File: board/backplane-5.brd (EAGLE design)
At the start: 100 x 100 mm, 142 parts, among them CN1 RJ45JACK90, U1 AMS1117-5.0, U10 RT9193, U11 KSZ9897, U12 KSZ8081MLX, U2 AMS1117-5.0, U3 AMS1117-5.0, U4 AMS1117-5.0, U5 AMS1117-5.0, U6 AMS1117-2.5, U7 AMS1117-1.2, U8 RT9193, U9 AMS1117-5.0, X1 25MHz, X2 25MHz

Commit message: Routed the MII interface
Holy shit.
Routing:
- net PHY6-CRS: track 0.00 -> 23.3 mm, vias 0 -> 2
- net PHY6-RXD0: track 0.00 -> 22.8 mm, vias 0 -> 2
- net PHY6-RXD2: track 0.00 -> 22.5 mm, vias 0 -> 2
- net PHY6-RXD1: track 0.00 -> 22.3 mm, vias 0 -> 2
- net PHY6-RXD3: track 0.00 -> 22.3 mm, vias 0 -> 2
- net PHY6-COL: track 0.00 -> 21.9 mm
- net PHY6-TXD3: track 0.00 -> 21.2 mm
- net PHY6-TXD2: track 0.00 -> 20.6 mm
- net PHY6-TXC: track 0.00 -> 16.9 mm, vias 0 -> 2
- net PHY6-RXER: track 0.00 -> 16.6 mm, vias 0 -> 2
- net PHY6-TXD1: track 0.00 -> 16.4 mm
- net PHY6-TXD0: track 0.00 -> 16.4 mm
- net PHY6-TXEN: track 0.00 -> 15.9 mm, vias 0 -> 2
- net PHY6-RXC: track 0.00 -> 15.7 mm
- net PHY6-RXDV: track 0.00 -> 15.6 mm
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
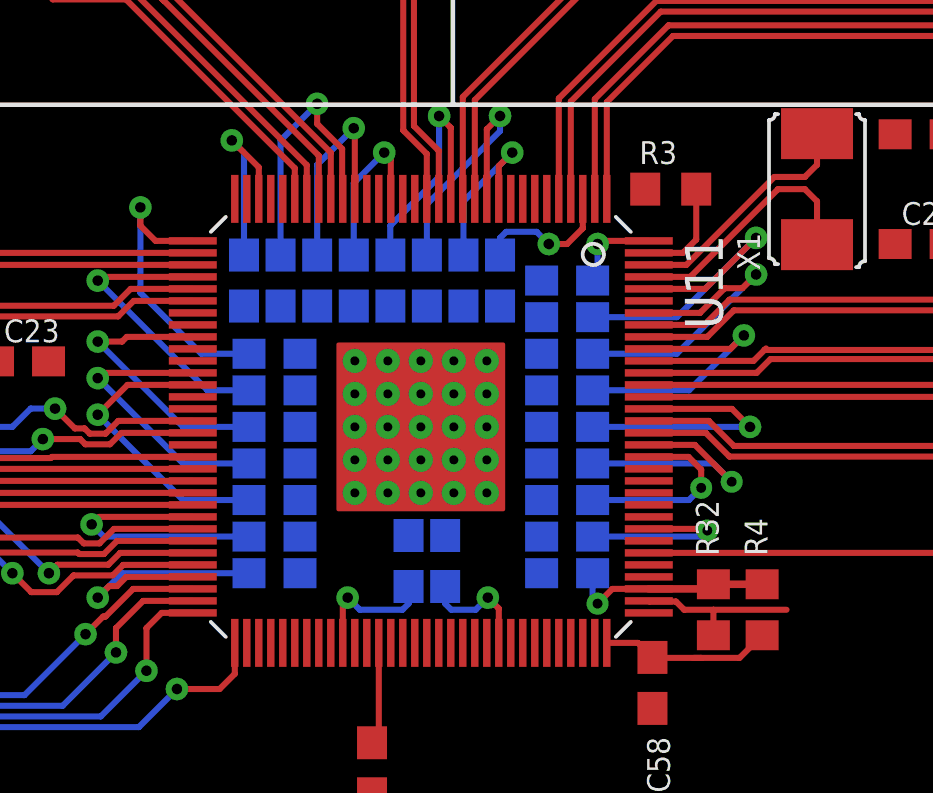
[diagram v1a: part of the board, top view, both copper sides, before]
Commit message: Tweaked some decoupling caps
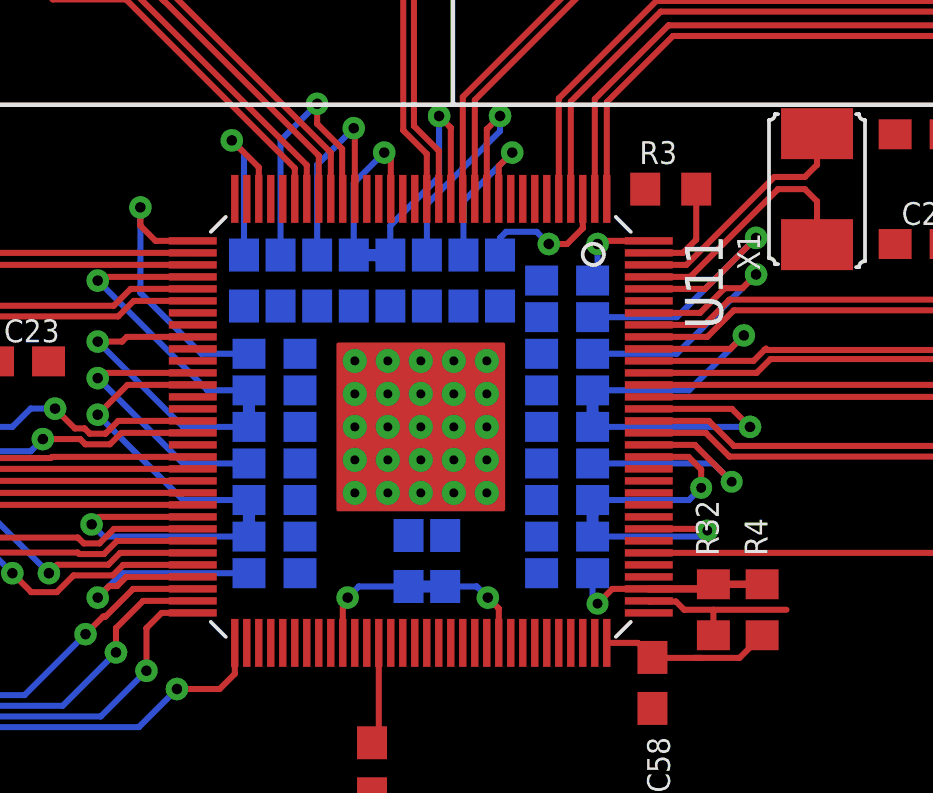
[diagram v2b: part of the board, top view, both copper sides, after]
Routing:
- net 1V2-A: track 72.9 -> 76.5 mm
- net 1V2: track 64.2 -> 66.5 mm
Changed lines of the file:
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@@
 <via x="68.4784" y="25.8064" extent="1-16" drill="0.3302"/>
 <via x="68.2752" y="27.2288" extent="1-16" drill="0.3302"/>
-<wire x1="64.6548" y1="25.6032" x2="68.2752" y2="25.6032" width="0.2032" layer="16"/>
+<wire x1="68.2752" y1="25.6032" x2="64.6548" y2="25.6032" width="0.2032" layer="16"/>
 <wire x1="68.2752" y1="25.6032" x2="68.4784" y2="25.8064" width="0.2032" layer="16"/>
 <wire x1="66.528" y1="25.8608" x2="68.424" y2="25.8608" width="0.2032" layer="1"/>
@@
 <wire x1="51.328" y1="30.6608" x2="49.152" y2="30.6608" width="0.2032" layer="1"/>
 <wire x1="49.152" y1="30.6608" x2="48.1584" y2="29.6672" width="0.2032" layer="1"/>
-<wire x1="53.2012" y1="26.8224" x2="51.0032" y2="26.8224" width="0.2032" layer="16"/>
+<wire x1="51.0032" y1="26.8224" x2="53.2012" y2="26.8224" width="0.2032" layer="16"/>
 <wire x1="51.0032" y1="26.8224" x2="48.1584" y2="29.6672" width="0.2032" layer="16"/>
 <via x="55.4736" y="40.0304" extent="1-16" drill="0.35"/>
@@
 <via x="61.1632" y="23.5712" extent="1-16" drill="0.35"/>
 <via x="56.4896" y="23.5712" extent="1-16" drill="0.35"/>
-<wire x1="58.5216" y1="23.9404" x2="58.5216" y2="23.368" width="0.2032" layer="16"/>
-<wire x1="58.5216" y1="23.368" x2="58.3184" y2="23.1648" width="0.2032" layer="16"/>
-<wire x1="58.3184" y1="23.1648" x2="56.896" y2="23.1648" width="0.2032" layer="16"/>
-<wire x1="56.896" y1="23.1648" x2="56.4896" y2="23.5712" width="0.2032" layer="16"/>
 <wire x1="56.328" y1="22.0608" x2="56.328" y2="23.4096" width="0.2032" layer="1"/>
 <wire x1="56.328" y1="23.4096" x2="56.4896" y2="23.5712" width="0.2032" layer="1"/>
-<wire x1="59.7408" y1="23.9404" x2="59.7408" y2="23.368" width="0.2032" layer="16"/>
-<wire x1="59.7408" y1="23.368" x2="59.944" y2="23.1648" width="0.2032" layer="16"/>
-<wire x1="59.944" y1="23.1648" x2="60.7568" y2="23.1648" width="0.2032" layer="16"/>
-<wire x1="60.7568" y1="23.1648" x2="61.1632" y2="23.5712" width="0.2032" layer="16"/>
 <wire x1="61.528" y1="22.0608" x2="61.528" y2="23.2064" width="0.2032" layer="1"/>
 <wire x1="61.528" y1="23.2064" x2="61.1632" y2="23.5712" width="0.2032" layer="1"/>
@@
 <wire x1="48.3616" y1="25.6032" x2="47.9552" y2="26.0096" width="0.2032" layer="16"/>
 <wire x1="53.2012" y1="25.6032" x2="48.3616" y2="25.6032" width="0.2032" layer="16"/>
+<wire x1="64.6548" y1="25.6032" x2="64.6548" y2="26.8224" width="0.4064" layer="16"/>
+<wire x1="53.2012" y1="26.8224" x2="53.2012" y2="25.6032" width="0.4064" layer="16"/>
+<wire x1="58.5216" y1="23.9404" x2="59.7408" y2="23.9404" width="0.4064" layer="16"/>
+<wire x1="58.5216" y1="23.9404" x2="56.8588" y2="23.9404" width="0.2032" layer="16"/>
+<wire x1="56.8588" y1="23.9404" x2="56.4896" y2="23.5712" width="0.2032" layer="16"/>
+<wire x1="59.7408" y1="23.9404" x2="60.794" y2="23.9404" width="0.2032" layer="16"/>
+<wire x1="60.794" y1="23.9404" x2="61.1632" y2="23.5712" width="0.2032" layer="16"/>
 <wire x1="-98.64" y1="-285.75" x2="-76.07" y2="-118.11" width="0" layer="19" extent="1-1"/>
 <wire x1="23.6084" y1="28.8544" x2="-76.07" y2="-118.11" width="0" layer="19" extent="1-1"/>
 <wire x1="35.9492" y1="27.0724" x2="27.4492" y2="28.0724" width="0" layer="19" extent="1-1"/>
 <wire x1="47.9552" y1="26.0096" x2="38.9772" y2="27.2288" width="0" layer="19" extent="1-1"/>
-<wire x1="51.0032" y1="26.8224" x2="51.328" y2="26.2608" width="0" layer="19" extent="1-16"/>
 <wire x1="56.328" y1="23.4096" x2="53.2012" y2="25.6032" width="0" layer="19" extent="1-16"/>
-<wire x1="59.7408" y1="23.9404" x2="58.5216" y2="23.9404" width="0" layer="19" extent="16-16"/>
 <wire x1="64.6548" y1="25.6032" x2="61.528" y2="23.2064" width="0" layer="19" extent="1-16"/>
-<wire x1="67.8688" y1="26.8224" x2="68.424" y2="25.8608" width="0" layer="19" extent="1-16"/>
 <wire x1="54.2544" y1="34.9876" x2="51.328" y2="30.6608" width="0" layer="19" extent="1-16"/>
 <wire x1="59.1312" y1="36.6827" x2="56.328" y2="36.8608" width="0" layer="19" extent="1-16"/>
@@
 <wire x1="66.528" y1="29.8608" x2="69.3008" y2="29.8608" width="0.2032" layer="1"/>
 <wire x1="69.3008" y1="29.8608" x2="69.9008" y2="29.2608" width="0.2032" layer="1"/>
-<wire x1="64.6548" y1="29.2608" x2="69.9008" y2="29.2608" width="0.2032" layer="16"/>
+<wire x1="69.9008" y1="29.2608" x2="64.6548" y2="29.2608" width="0.2032" layer="16"/>
 <via x="69.6976" y="32.3088" extent="1-16" drill="0.35"/>
 <wire x1="66.528" y1="31.8608" x2="69.2496" y2="31.8608" width="0.2032" layer="1"/>
@@
 <wire x1="51.328" y1="34.2608" x2="48.2816" y2="34.2608" width="0.2032" layer="1"/>
 <wire x1="48.2816" y1="34.2608" x2="48.1584" y2="34.1376" width="0.2032" layer="1"/>
-<wire x1="53.2012" y1="30.48" x2="51.816" y2="30.48" width="0.2032" layer="16"/>
+<wire x1="51.816" y1="30.48" x2="53.2012" y2="30.48" width="0.2032" layer="16"/>
 <wire x1="51.816" y1="30.48" x2="48.1584" y2="34.1376" width="0.2032" layer="16"/>
 <via x="52.6288" y="38.8112" extent="1-16" drill="0.35"/>
@@
 <wire x1="57.928" y1="36.8608" x2="57.928" y2="38.1856" width="0.2032" layer="1"/>
 <wire x1="57.928" y1="38.1856" x2="57.7088" y2="38.4048" width="0.2032" layer="1"/>
-<wire x1="56.6928" y1="34.9876" x2="56.6928" y2="37.3888" width="0.2032" layer="16"/>
+<wire x1="56.6928" y1="37.3888" x2="56.6928" y2="34.9876" width="0.2032" layer="16"/>
 <wire x1="56.6928" y1="37.3888" x2="57.7088" y2="38.4048" width="0.2032" layer="16"/>
 <via x="59.5376" y="39.624" extent="1-16" drill="0.35"/>
 <wire x1="59.928" y1="36.8608" x2="59.928" y2="39.2336" width="0.2032" layer="1"/>
 <wire x1="59.928" y1="39.2336" x2="59.5376" y2="39.624" width="0.2032" layer="1"/>
-<wire x1="57.912" y1="34.9876" x2="57.912" y2="35.9664" width="0.2032" layer="16"/>
+<wire x1="57.912" y1="35.9664" x2="57.912" y2="34.9876" width="0.2032" layer="16"/>
 <wire x1="57.912" y1="35.9664" x2="59.5376" y2="37.592" width="0.2032" layer="16"/>
 <wire x1="59.5376" y1="37.592" x2="59.5376" y2="39.624" width="0.2032" layer="16"/>
@@
 <wire x1="64.6548" y1="32.9184" x2="67.4624" y2="32.9184" width="0.2032" layer="16"/>
 <wire x1="67.4624" y1="32.9184" x2="70.104" y2="35.56" width="0.2032" layer="16"/>
+<wire x1="64.6548" y1="29.2608" x2="64.6548" y2="30.48" width="0.4064" layer="16"/>
+<wire x1="57.912" y1="34.9876" x2="56.6928" y2="34.9876" width="0.4064" layer="16"/>
+<wire x1="53.2012" y1="30.48" x2="53.2012" y2="29.2608" width="0.4064" layer="16"/>
 <wire x1="-85.94" y1="-219.71" x2="-78.87" y2="-118.11" width="0" layer="19" extent="1-1"/>
 <wire x1="44.8192" y1="31.4452" x2="-78.87" y2="-118.11" width="0" layer="19" extent="1-1"/>

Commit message: Routed some config resistors
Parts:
- moved R31 548.0 mm to (38.6, 16.9), turned to 90 degrees
- moved R30 541.9 mm to (35.2, 16.7), turned to 90 degrees
- moved R29 536.6 mm to (33.5, 16.7), turned to 90 degrees
- moved R6 381.3 mm to (29.5, 35.4), turned to 90 degrees
- moved C68 373.5 mm to (28.4, 32.9), turned to 180 degrees
- moved C23 0.59 mm to (45.4, 32.0), turned to 180 degrees
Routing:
- net PHY5LED1: track 0.00 -> 45.7 mm
- net N$12: track 0.00 -> 3.57 mm
- net PHY6-RXD0: track 22.8 -> 25.8 mm
- net PHY6-RXD3: track 22.3 -> 24.9 mm
- net PHY6-RXD2: track 22.5 -> 24.9 mm
- net 1V2-A: track 76.5 -> 78.5 mm
- net 1V2: track 66.5 -> 67.2 mm

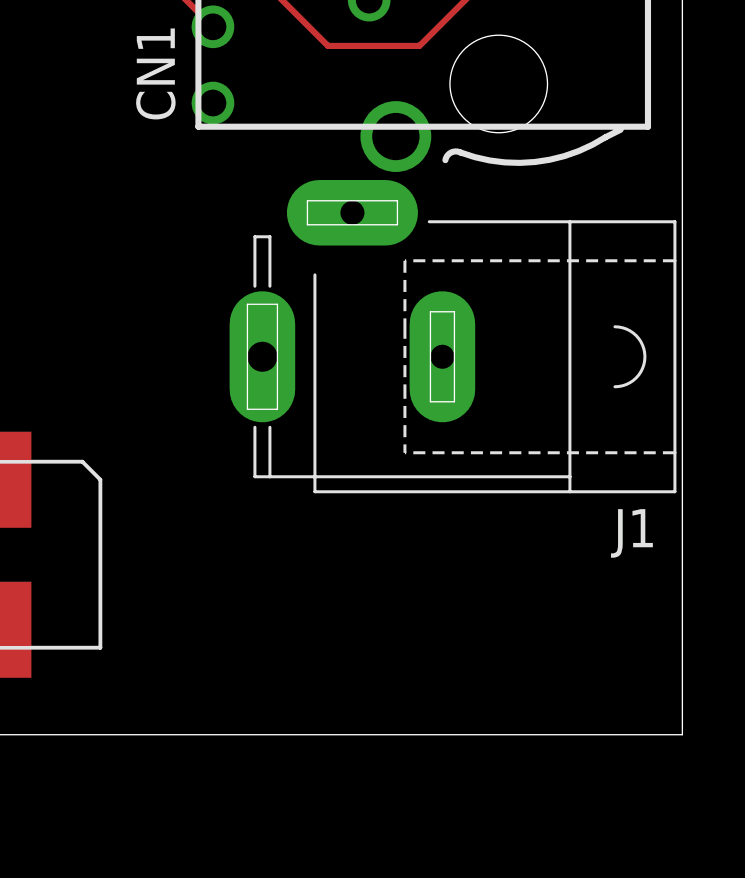
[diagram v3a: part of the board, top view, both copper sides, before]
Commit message: Tweaked some traces and updated the library
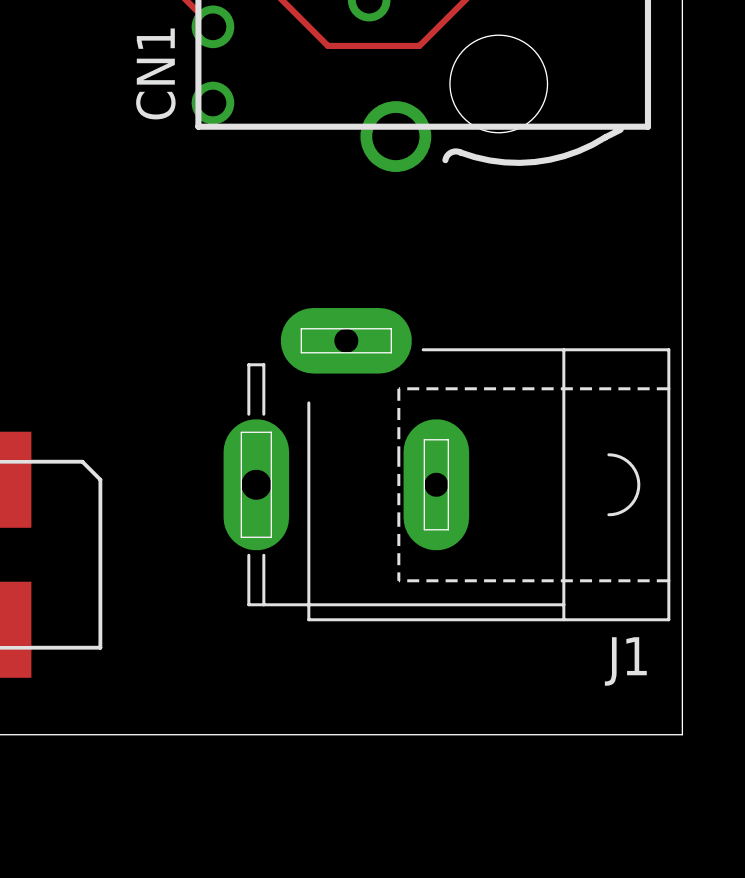
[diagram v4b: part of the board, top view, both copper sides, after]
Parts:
- moved J1 4.27 mm to (88.8, 8.33)
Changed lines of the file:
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@@
 <?xml version="1.0" encoding="utf-8"?>
 <!DOCTYPE eagle SYSTEM "eagle.dtd">
-<eagle version="8.3.2">
+<eagle version="8.3.1">
 <drawing>
 <settings>
@@
 <attribute name="NAME" x="9" y="67" size="0.635" layer="21" rot="R180" align="top-left"/>
 </element>
-<element name="J1" library="tuetuopay" package="SPC4077" value="" x="89.0016" y="12.5984" rot="R180">
-<attribute name="MF" value="" x="89.0016" y="12.5984" size="1.778" layer="27" rot="R180" display="off"/>
-<attribute name="MPN" value="" x="89.0016" y="12.5984" size="1.778" layer="27" rot="R180" display="off"/>
-<attribute name="OC_FARNELL" value="unknown" x="89.0016" y="12.5984" size="1.778" layer="27" rot="R180" display="off"/>
-<attribute name="OC_NEWARK" value="unknown" x="89.0016" y="12.5984" size="1.778" layer="27" rot="R180" display="off"/>
+<element name="J1" library="tuetuopay" package="SPC4077" value="" x="88.7984" y="8.3312" rot="R180">
+<attribute name="MF" value="" x="88.7984" y="8.3312" size="1.778" layer="27" rot="R180" display="off"/>
+<attribute name="MPN" value="" x="88.7984" y="8.3312" size="1.778" layer="27" rot="R180" display="off"/>
+<attribute name="OC_FARNELL" value="unknown" x="88.7984" y="8.3312" size="1.778" layer="27" rot="R180" display="off"/>
+<attribute name="OC_NEWARK" value="unknown" x="88.7984" y="8.3312" size="1.778" layer="27" rot="R180" display="off"/>
 </element>
 <element name="R1" library="rcl" library_urn="urn:adsk.eagle:library:334" package="R0603" package3d_urn="urn:adsk.eagle:package:23555/2" value="1k" x="11.7856" y="18.6944" smashed="yes" rot="R270">
@@
 <wire x1="31.5" y1="63" x2="30.95" y2="68.7" width="0" layer="19" extent="1-1"/>
 <wire x1="10.95" y1="68.7" x2="30.95" y2="68.7" width="0" layer="19" extent="1-1"/>
-<wire x1="86.0016" y1="12.5984" x2="91.5" y2="63" width="0" layer="19" extent="1-1"/>
-<wire x1="68.2" y1="8.05" x2="86.0016" y2="12.5984" width="0" layer="19" extent="1-1"/>
+<wire x1="85.7984" y1="8.3312" x2="91.5" y2="63" width="0" layer="19" extent="1-1"/>
+<wire x1="68.2" y1="8.05" x2="85.7984" y2="8.3312" width="0" layer="19" extent="1-1"/>
 <wire x1="63.5" y1="8.5" x2="68.2" y2="8.05" width="0" layer="19" extent="1-1"/>
 <wire x1="47.2" y1="7.55" x2="63.5" y2="8.5" width="0" layer="19" extent="1-1"/>
@@
 <wire x1="90.4494" y1="36.1442" x2="76.4404" y2="35.3568" width="0" layer="19" extent="1-1"/>
 <wire x1="90.4494" y1="19.939" x2="90.4494" y2="36.1442" width="0" layer="19" extent="1-1"/>
-<wire x1="92.0016" y1="12.5984" x2="90.4494" y2="19.939" width="0" layer="19" extent="1-1"/>
+<wire x1="91.7984" y1="8.3312" x2="90.4494" y2="19.939" width="0" layer="19" extent="1-1"/>
 <wire x1="76.5" y1="63" x2="76.4404" y2="39.0144" width="0" layer="19" extent="1-1"/>
 <wire x1="70.95" y1="73.3" x2="76.5" y2="63" width="0" layer="19" extent="1-1"/>

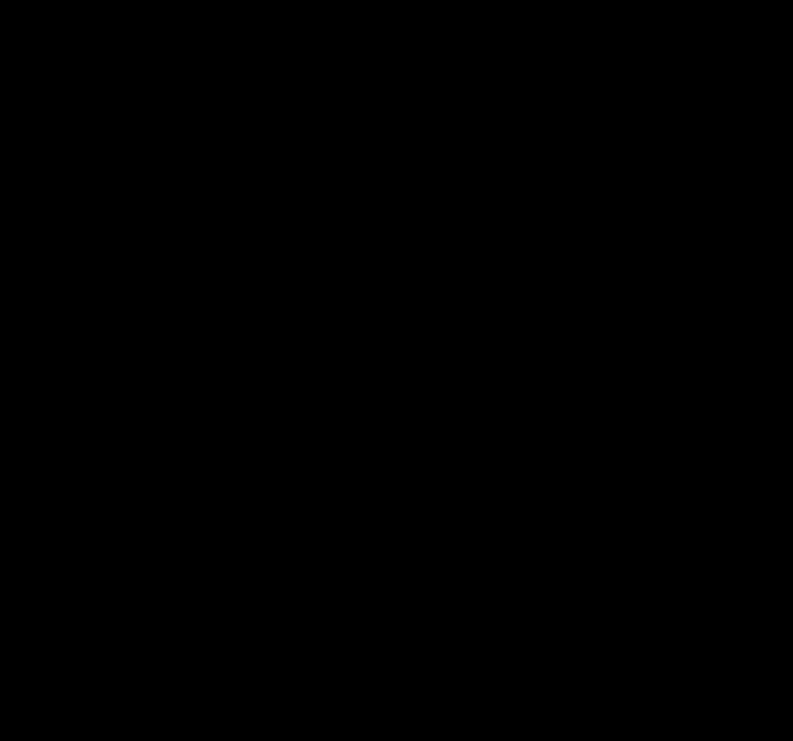
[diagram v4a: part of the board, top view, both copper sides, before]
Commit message: Added STM32F217
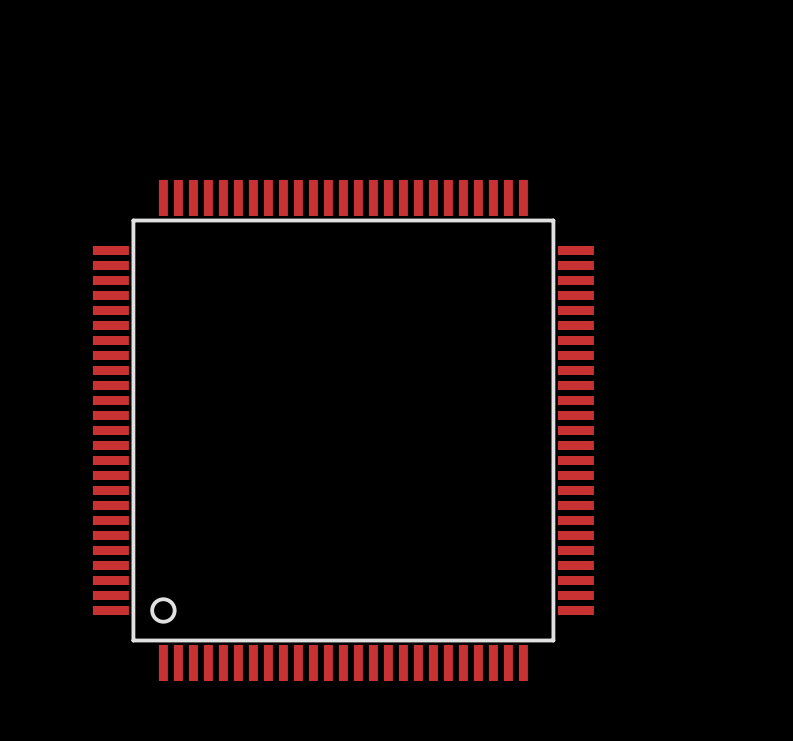
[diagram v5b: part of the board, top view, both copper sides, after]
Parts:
- added U13: STM32F217-100, tuetuopay:LQFP-100
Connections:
- net 3V3-LED renamed 3V3-STM32
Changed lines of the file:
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@@
 <attribute name="NAME" x="68.8594" y="24.9682" size="0.762" layer="25" rot="R90"/>
 </element>
+<element name="U13" library="tuetuopay" package="LQFP-100" value="STM32F217-100" x="-138.3792" y="-526.288"/>
 </elements>
 <signals>
@@
 <wire x1="49.5" y1="7.55" x2="49.95" y2="9.7536" width="0" layer="19" extent="1-1"/>
 </signal>
-<signal name="3V3-LED">
+<signal name="3V3-STM32">
 <contactref element="U8" pad="5"/>
 <contactref element="C16" pad="1"/>
